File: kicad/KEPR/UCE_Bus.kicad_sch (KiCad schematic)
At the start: 2 parts, among them J1 SODIMM-200, J2 SODIMM-200

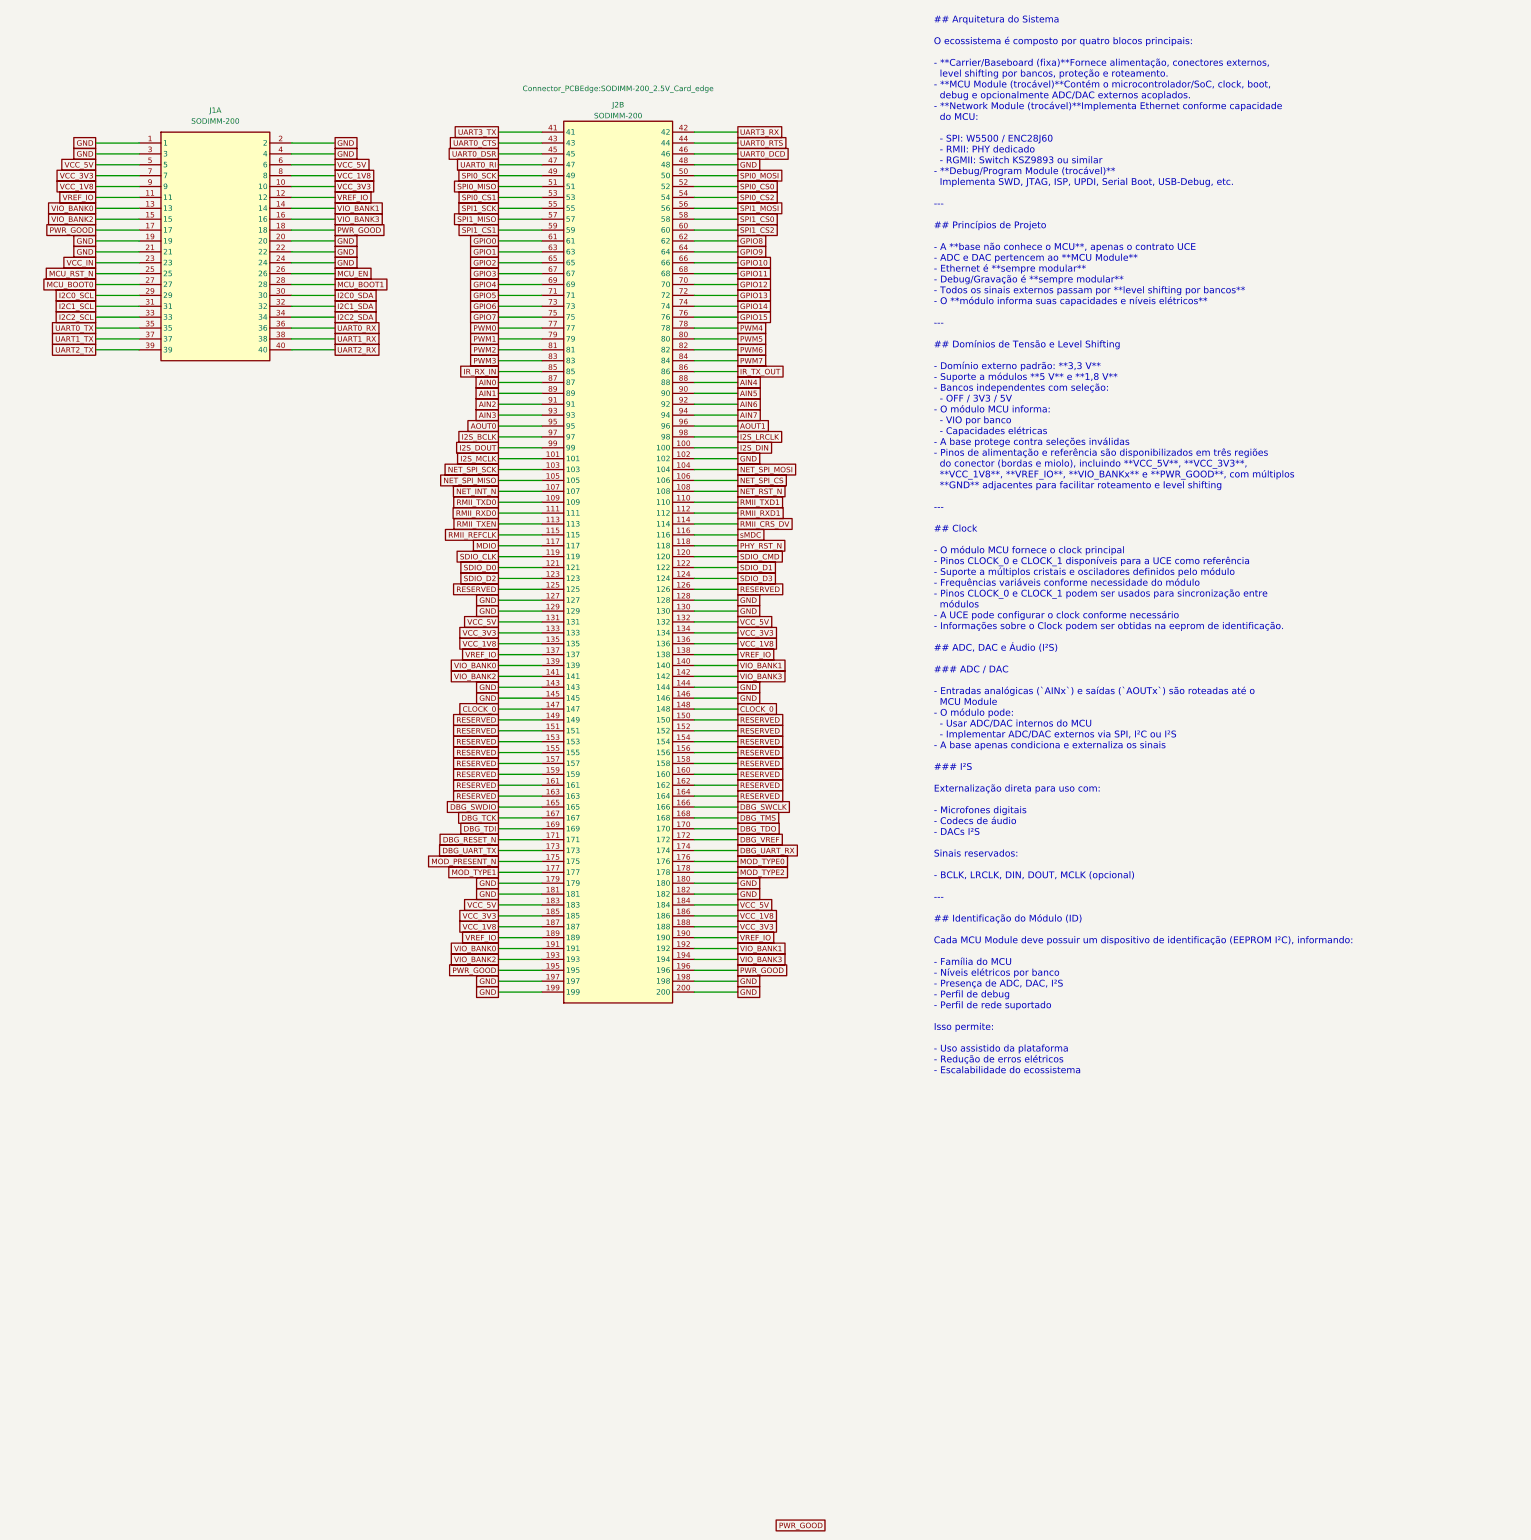
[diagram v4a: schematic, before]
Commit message: Vários ajuste, sendo o mais importante a adição do power rail e iniciado o Wireless module
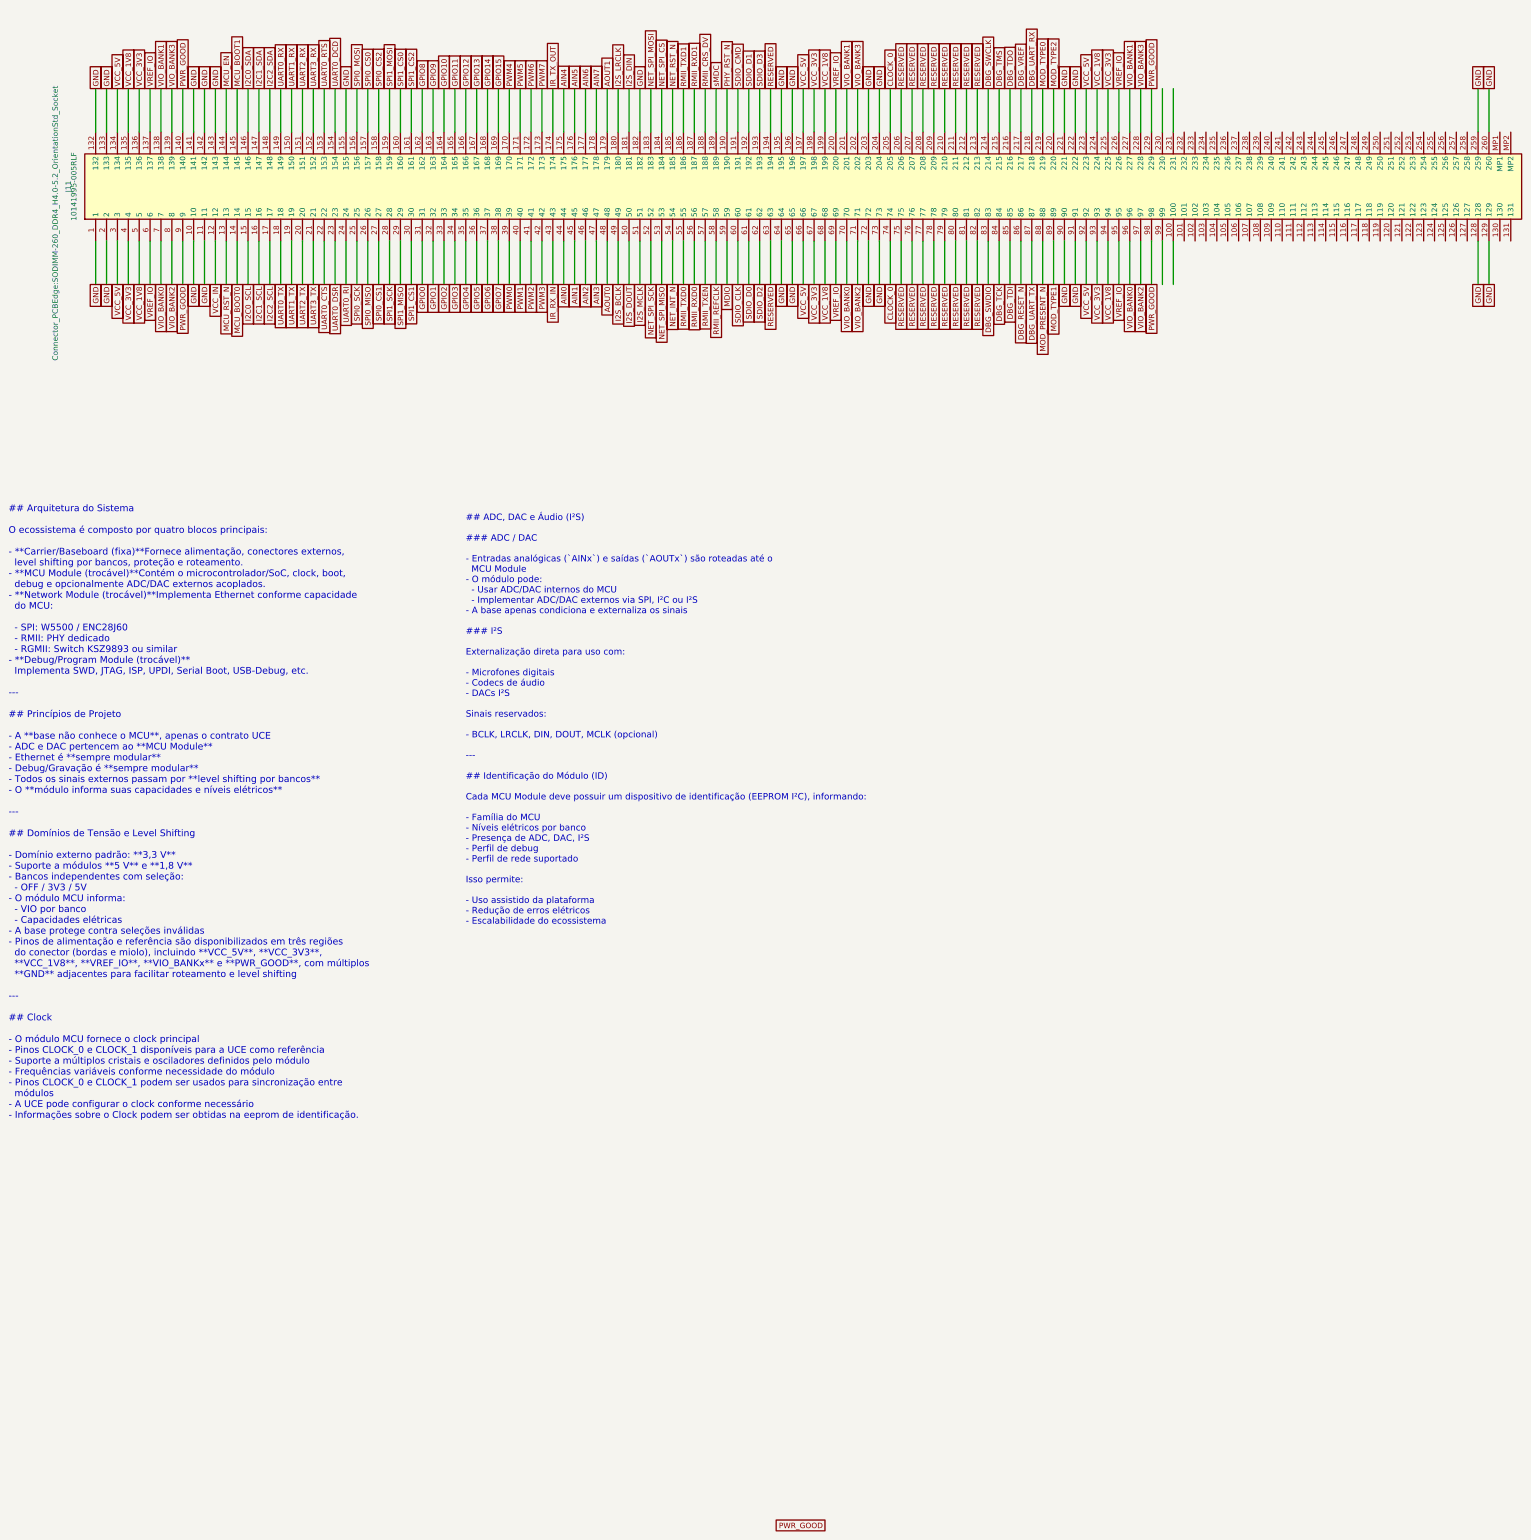
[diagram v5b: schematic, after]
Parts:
- removed J1: SODIMM-200, symbol Connector:SODIMM-200
- removed J2: SODIMM-200, Connector_PCBEdge:SODIMM-200_2.5V_Card_edge, symbol Connector:SODIMM-200
- added J11: 10141995-005RLF, Connector_PCBEdge:SODIMM-260_DDR4_H4.0-5.2_OrientationStd_Socket, symbol 10141995-005RLF:10141995-005RLF
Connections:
- net AIN0: now also J11.44
- net AIN1: now also J11.45
- net AIN2: now also J11.46
- net AIN3: now also J11.47
- net AIN4: now also J11.175
- net AIN5: now also J11.176
- net AIN6: now also J11.177
- net AIN7: now also J11.178
- net AOUT0: now also J11.48
- net AOUT1: now also J11.179
- net CLOCK_0: now also J11.205, J11.74
- net DBG_RESET_N: now also J11.86
- net DBG_SWCLK: now also J11.214
- net DBG_SWDIO: now also J11.83
- net DBG_TCK: now also J11.84
- net DBG_TDI: now also J11.85
- net DBG_TDO: now also J11.216
- net DBG_TMS: now also J11.215
- net DBG_UART_RX: now also J11.218
- net DBG_UART_TX: now also J11.87
- net DBG_VREF: now also J11.217
- net GND: now also J11.1, J11.10, J11.11, J11.128, J11.129, J11.132, J11.133, J11.141, J11.142, J11.143, J11.155, J11.182, J11.195, J11.196, J11.2, J11.203, J11.204, J11.221, J11.222, J11.259, J11.260, J11.64, J11.65, J11.72, J11.73, J11.90, J11.91
- net GPIO0: now also J11.31
- net GPIO1: now also J11.32
- net GPIO10: now also J11.164
- net GPIO11: now also J11.165
- net GPIO12: now also J11.166
- net GPIO13: now also J11.167
- net GPIO14: now also J11.168
- net GPIO15: now also J11.169
- net GPIO2: now also J11.33
- net GPIO3: now also J11.34
- net GPIO4: now also J11.35
- net GPIO5: now also J11.36
- net GPIO6: now also J11.37
- net GPIO7: now also J11.38
- net GPIO8: now also J11.162
- net GPIO9: now also J11.163
- net I2C0_SCL: now also J11.15
- net I2C0_SDA: now also J11.146
- net I2C1_SCL: now also J11.16
- net I2C1_SDA: now also J11.147
- net I2C2_SCL: now also J11.17
- net I2C2_SDA: now also J11.148
- net I2S_BCLK: now also J11.49
- net I2S_DIN: now also J11.181
- net I2S_DOUT: now also J11.50
- net I2S_LRCLK: now also J11.180
- net I2S_MCLK: now also J11.51
- net IR_RX_IN: now also J11.43
- net IR_TX_OUT: now also J11.174
- net MCU_BOOT0: now also J11.14
- net MCU_BOOT1: now also J11.145
- net MCU_EN: now also J11.144
- net MCU_RST_N: now also J11.13
- net MDIO: now also J11.59
- net MOD_PRESENT_N: now also J11.88
- net MOD_TYPE0: now also J11.219
- net MOD_TYPE1: now also J11.89
- net MOD_TYPE2: now also J11.220
- net NET_INT_N: now also J11.54
- net NET_RST_N: now also J11.185
- net NET_SPI_CS: now also J11.184
- net NET_SPI_MISO: now also J11.53
- net NET_SPI_MOSI: now also J11.183
- net NET_SPI_SCK: now also J11.52
- net PHY_RST_N: now also J11.190
- net PWM0: now also J11.39
- net PWM1: now also J11.40
- net PWM2: now also J11.41
- net PWM3: now also J11.42
- net PWM4: now also J11.170
- net PWM5: now also J11.171
- net PWM6: now also J11.172
- net PWM7: now also J11.173
- net PWR_GOOD: now also J11.140, J11.229, J11.9, J11.98
- net RESERVED: now also J11.194, J11.206, J11.207, J11.208, J11.209, J11.210, J11.211, J11.212, J11.213, J11.63, J11.75, J11.76, J11.77, J11.78, J11.79, J11.80, J11.81, J11.82
- net RMII_CRS_DV: now also J11.188
- net RMII_REFCLK: now also J11.58
- net RMII_RXD0: now also J11.56
- net RMII_RXD1: now also J11.187
- net RMII_TXD0: now also J11.55
- net RMII_TXD1: now also J11.186
- net RMII_TXEN: now also J11.57
- net SDIO_CLK: now also J11.60
- net SDIO_CMD: now also J11.191
- net SDIO_D0: now also J11.61
- net SDIO_D1: now also J11.192
- net SDIO_D2: now also J11.62
- net SDIO_D3: now also J11.193
- net SPI0_CS0: now also J11.157
- net SPI0_CS1: now also J11.27
- net SPI0_CS2: now also J11.158
- net SPI0_MISO: now also J11.26
- net SPI0_MOSI: now also J11.156
- net SPI0_SCK: now also J11.25
- net SPI1_CS0: now also J11.160
- net SPI1_CS1: now also J11.30
- net SPI1_CS2: now also J11.161
- net SPI1_MISO: now also J11.29
- net SPI1_MOSI: now also J11.159
- net SPI1_SCK: now also J11.28
- net UART0_CTS: now also J11.22
- net UART0_DCD: now also J11.154
- net UART0_DSR: now also J11.23
- net UART0_RI: now also J11.24
- net UART0_RTS: now also J11.153
- net UART0_RX: now also J11.149
- net UART0_TX: now also J11.18
- net UART1_RX: now also J11.150
- net UART1_TX: now also J11.19
- net UART2_RX: now also J11.151
- net UART2_TX: now also J11.20
- net UART3_RX: now also J11.152
- net UART3_TX: now also J11.21
- net VCC_1V8: now also J11.135, J11.199, J11.224, J11.5, J11.68, J11.94
- net VCC_3V3: now also J11.136, J11.198, J11.225, J11.4, J11.67, J11.93
- net VCC_5V: now also J11.134, J11.197, J11.223, J11.3, J11.66, J11.92
- net VCC_IN: now also J11.12
- net VIO_BANK0: now also J11.7, J11.70, J11.96
- net VIO_BANK1: now also J11.138, J11.201, J11.227
- net VIO_BANK2: now also J11.71, J11.8, J11.97
- net VIO_BANK3: now also J11.139, J11.202, J11.228
- net VREF_IO: now also J11.137, J11.200, J11.226, J11.6, J11.69, J11.95
- net sMDC: now also J11.189
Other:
- note added: "## ADC, DAC e Áudio (I²S) ### ADC / DAC - Entradas analógicas (`AINx`) e saídas (`AOUTx`) são roteadas até o MCU Module - O módulo pode: - Usar ADC/DAC internos do MCU - Implementar ADC/DAC externos via SPI, I²C ou I²S - A base apenas condiciona e externaliza os sinais ### I²S Externalização direta para uso com: - Microfones digitais - Codecs de áudio - DACs I²S Sinais reservados: - BCLK, LRCLK, 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"

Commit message: Ajustes no Power Rail, entre outros ajustes.
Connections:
- net I2C_SDA_MCU_CTL: now reaches J11.100
- net I2C_SCL_MCU_CTL: now reaches J11.99
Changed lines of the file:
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@@
+		)
+	)
+	(global_label "I2C_SDA_MCU_CTL"
+		(shape passive)
+		(at 297.18 83.82 270)
+		(fields_autoplaced yes)
+		(effects
+			(font
+				(size 1.27 1.27)
+			)
+			(justify right)
+		)
+		(property "Intersheetrefs" "${INTERSHEET_REFS}"
+			(at 297.18 102.5667 90)
+			(effects
+				(font
+					(size 1.27 1.27)
+				)
+				(justify right)
+				(hide yes)
+			)
 		)
 	)
@@
 				(hide yes)
 			)
+		)
+	)
+	(global_label "I2C_SCL_MCU_CTL"
+		(shape passive)
+		(at 294.64 83.82 270)
+		(fields_autoplaced yes)
+		(effects
+			(font
+				(size 1.27 1.27)
+			)
+			(justify right)
+		)
+		(property "Intersheetrefs" "${INTERSHEET_REFS}"
+			(at 294.64 102.5062 90)
+			(effects
+				(font
+					(size 1.27 1.27)
+				)
+				(justify right)
+				(hide yes)
+			)

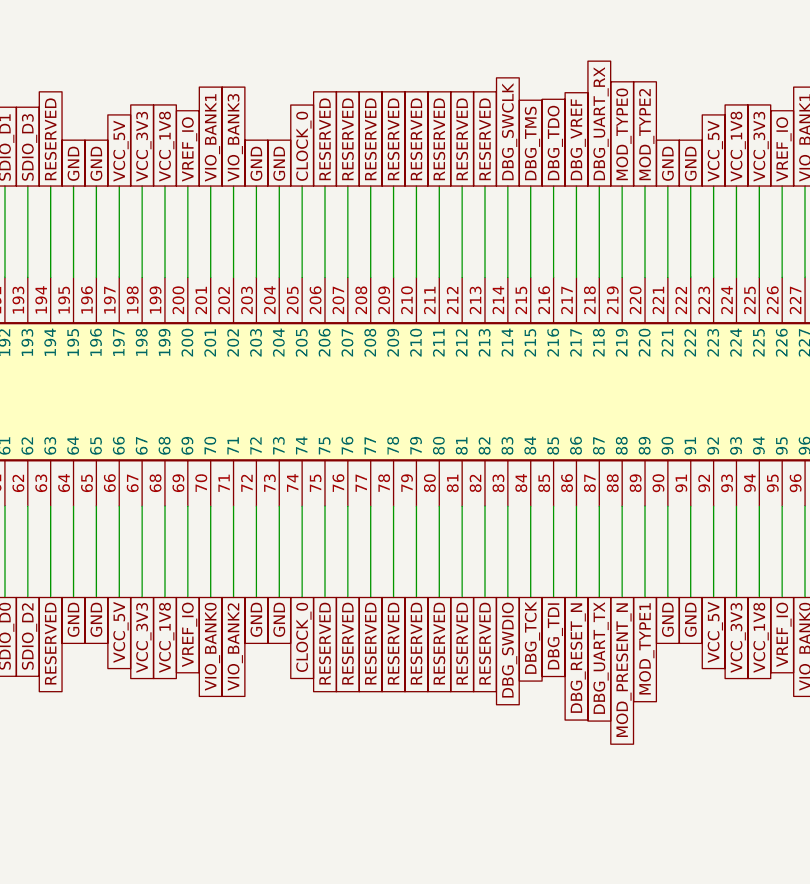
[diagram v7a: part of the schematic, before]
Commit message: Diversos ajustes no barramento e ampliação das trilhas na PCB
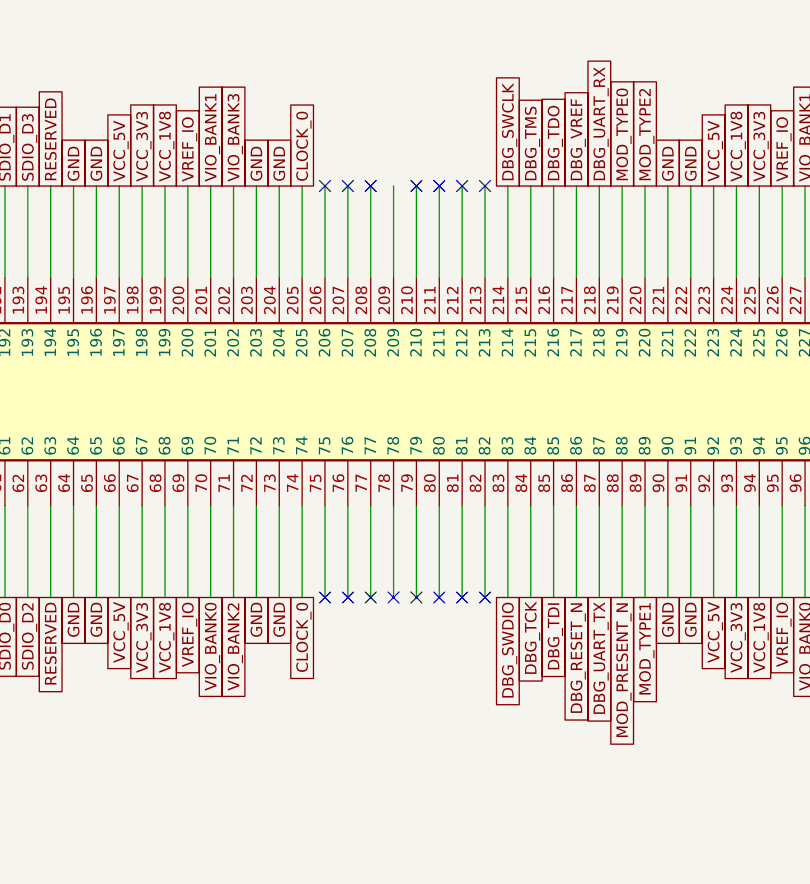
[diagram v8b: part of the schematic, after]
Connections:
- net RESERVED: no longer J11.206, J11.207, J11.208, J11.209, J11.210, J11.211, J11.212, J11.213, J11.75, J11.76, J11.77, J11.78, J11.79, J11.80, J11.81, J11.82
- no-connect marks 0 -> 15
